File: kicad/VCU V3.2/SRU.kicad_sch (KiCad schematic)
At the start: 23 parts, among them U10 40106, U11 LTV-847S

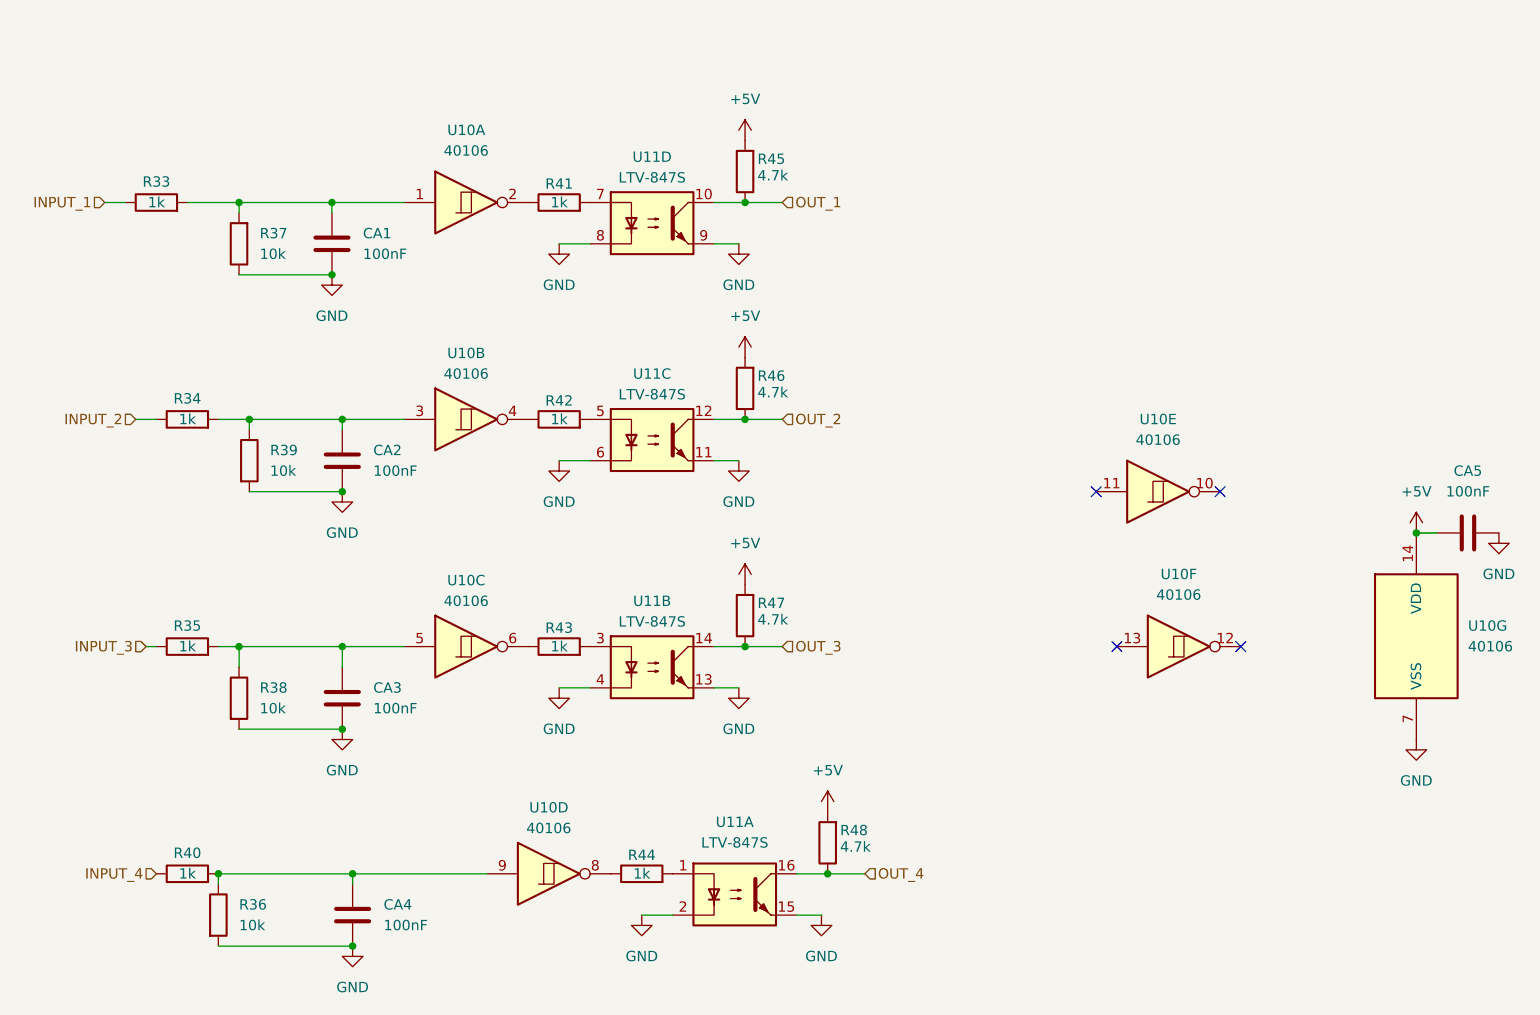
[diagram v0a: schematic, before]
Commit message: what
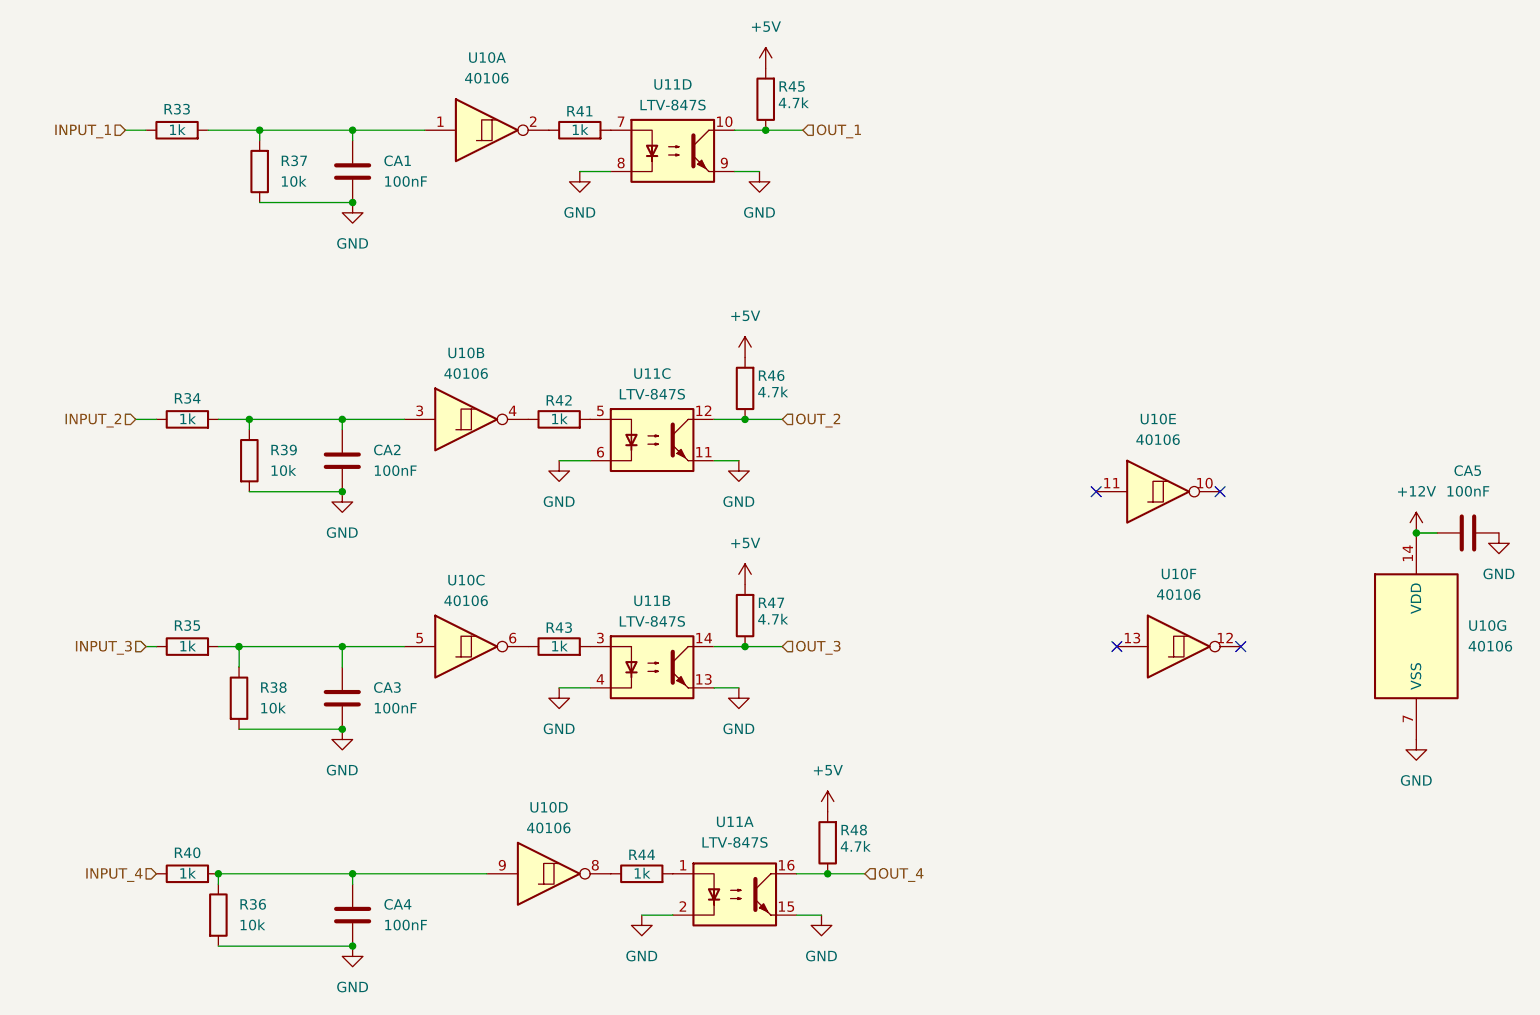
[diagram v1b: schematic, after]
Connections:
- net +5V: no longer CA5.1, U10.14 (VDD)
- new net +12V: CA5.1, U10.14 (VDD)
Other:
- moved on the sheet: CA1, R33, R37, R41, R45, U10A, U11D
